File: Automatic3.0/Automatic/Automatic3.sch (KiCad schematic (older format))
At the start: 66 parts, among them J1 GND_VCC, J10 Line Tracker and Proximity, J11 J, J12 Bluetooth, J13 Encoder, J14 J, J15 Motor, J19 J, J2 CONN_01X01, J20 Bluetooth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

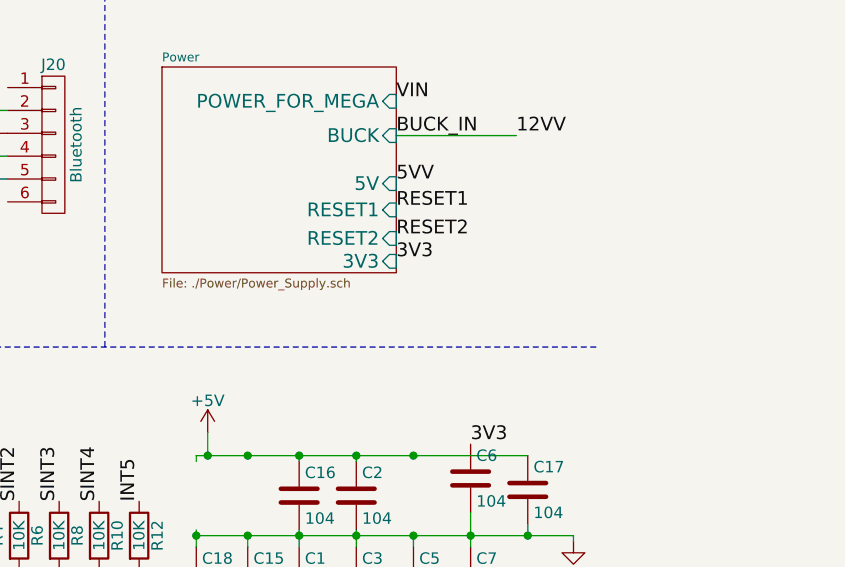
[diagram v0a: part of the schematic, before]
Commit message: Buck circuit also modified and pdfs also changed
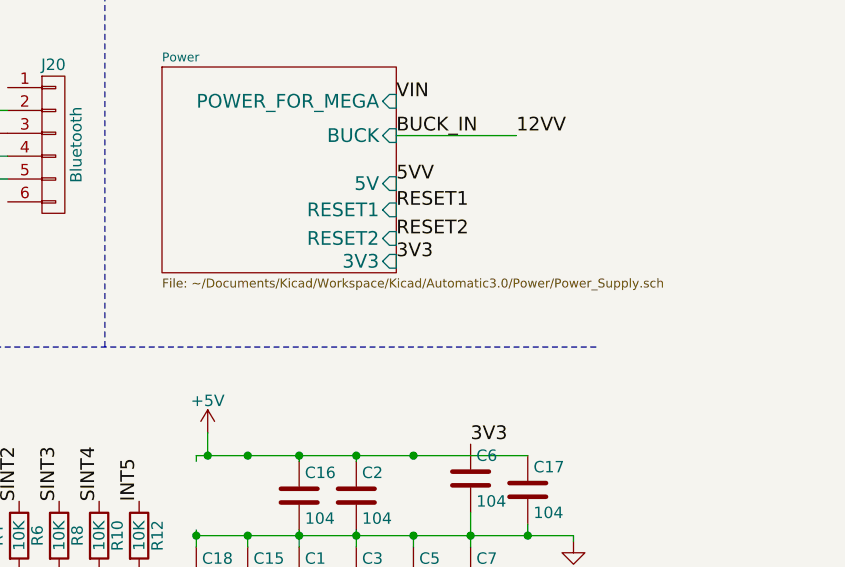
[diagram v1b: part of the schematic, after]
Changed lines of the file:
@@
 U 5B15B5AD
 F0 "Power" 39
-F1 "./Power/Power_Supply.sch" 39
+F1 "~/Documents/Kicad/Workspace/Kicad/Automatic3.0/Power/Power_Supply.sch" 39
 F2 "POWER_FOR_MEGA" I R 10350 950 60
 F3 "BUCK" I R 10350 1100 60

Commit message: added the minor project file
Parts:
- C1, C11, C12, C14, C15, C16, C17, C18, C2, C3, C5, C6, C7, C8: symbol C -> Automatic3-rescue:C
- D14, D4: symbol LED -> Automatic3-rescue:LED
- D2, D3: symbol D -> Automatic3-rescue:D
- J1: symbol Conn_02x03_Odd_Even -> Automatic3-rescue:Conn_02x03_Odd_Even
- J10, J13, J15: symbol DB15_FEMALE_MountingHoles -> Automatic3-rescue:DB15_FEMALE_MountingHoles
- J11, J14, J19, J21, J22: symbol J -> Automatic3-rescue:J
- J12, J20: symbol CONN_01X06 -> Automatic3-rescue:CONN_01X06
- J2, J24, J4, J5, J8: symbol CONN_01X01 -> Automatic3-rescue:CONN_01X01
- J23: symbol Conn_01x12 -> Automatic3-rescue:Conn_01x12
- J25, J7, J9: symbol Conn_01x04 -> Automatic3-rescue:Conn_01x04
- J26, J27: symbol CONN_01X02 -> Automatic3-rescue:CONN_01X02
- J3, J6: symbol DB9_Female_MountingHoles -> Automatic3-rescue:DB9_Female_MountingHoles
- R1, R10, R11, R12, R13, R2, R23, R24, R25, R26, R28, R3, R31, R32, R33, R34, R4, R5, R6, R7, R8, R9: symbol R -> Automatic3-rescue:R
- U1, U2: symbol Arduino_Mega2560_Shield -> Automatic3-rescue:Arduino_Mega2560_Shield
